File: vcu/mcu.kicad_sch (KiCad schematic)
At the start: 45 parts, among them J16 Spare pins, J7 Conn_ARM_JTAG_SWD_20, SW1 SW_Push, SW2 SW_SPDT, U7 STM32F746ZGT6, U8 LD1117S33TR_SOT223, Y1 8MHz

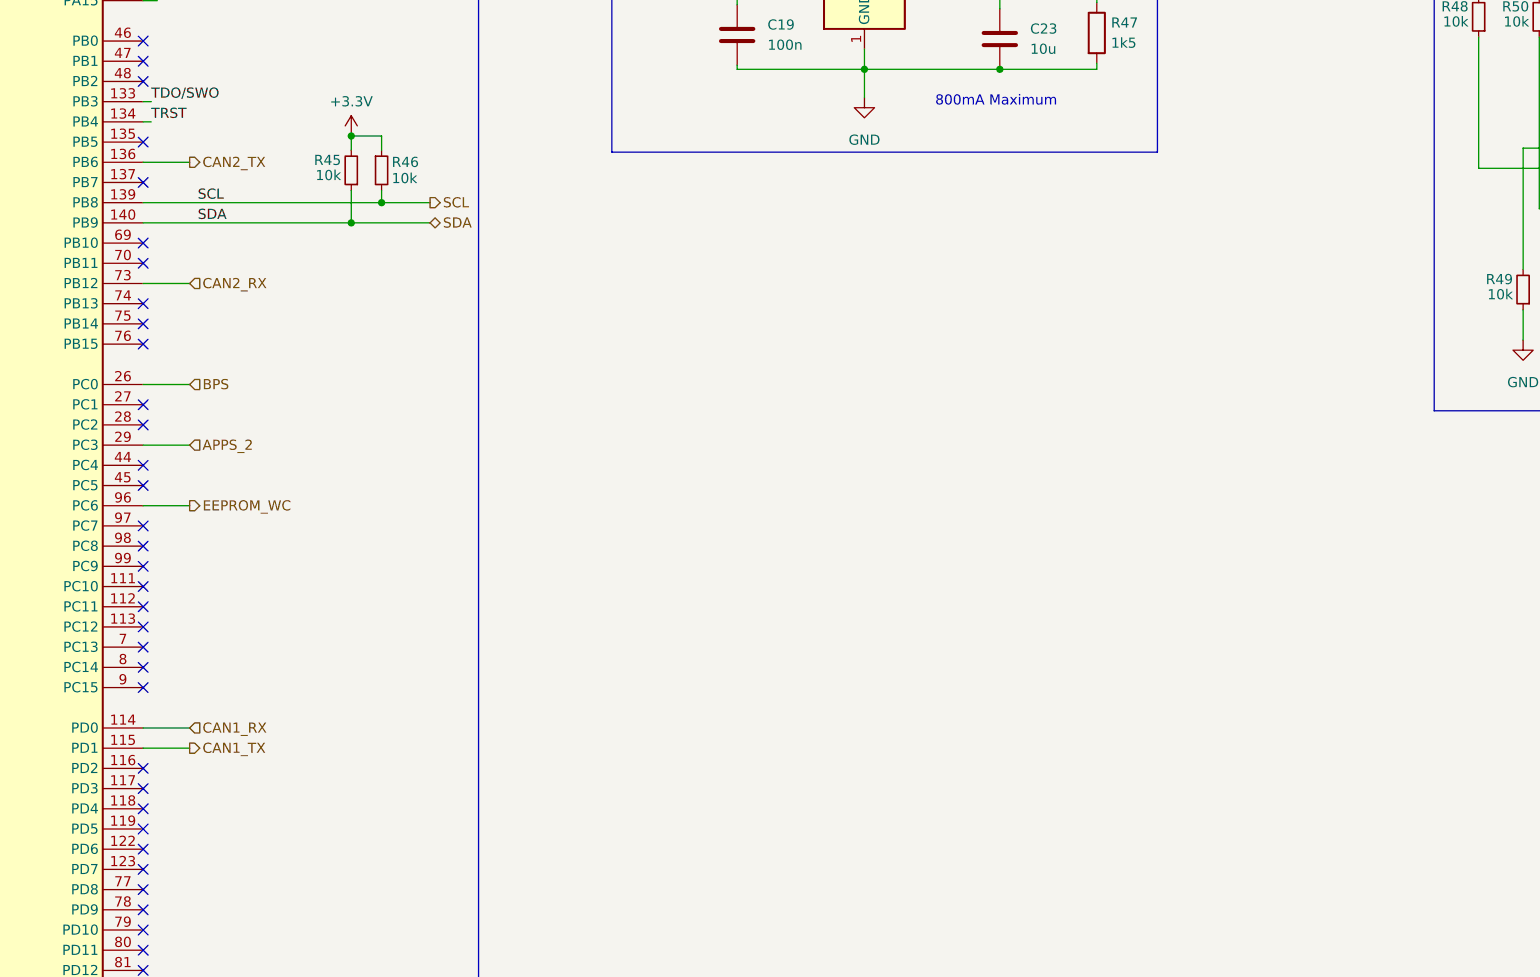
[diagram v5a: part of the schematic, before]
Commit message: Fixed CAN
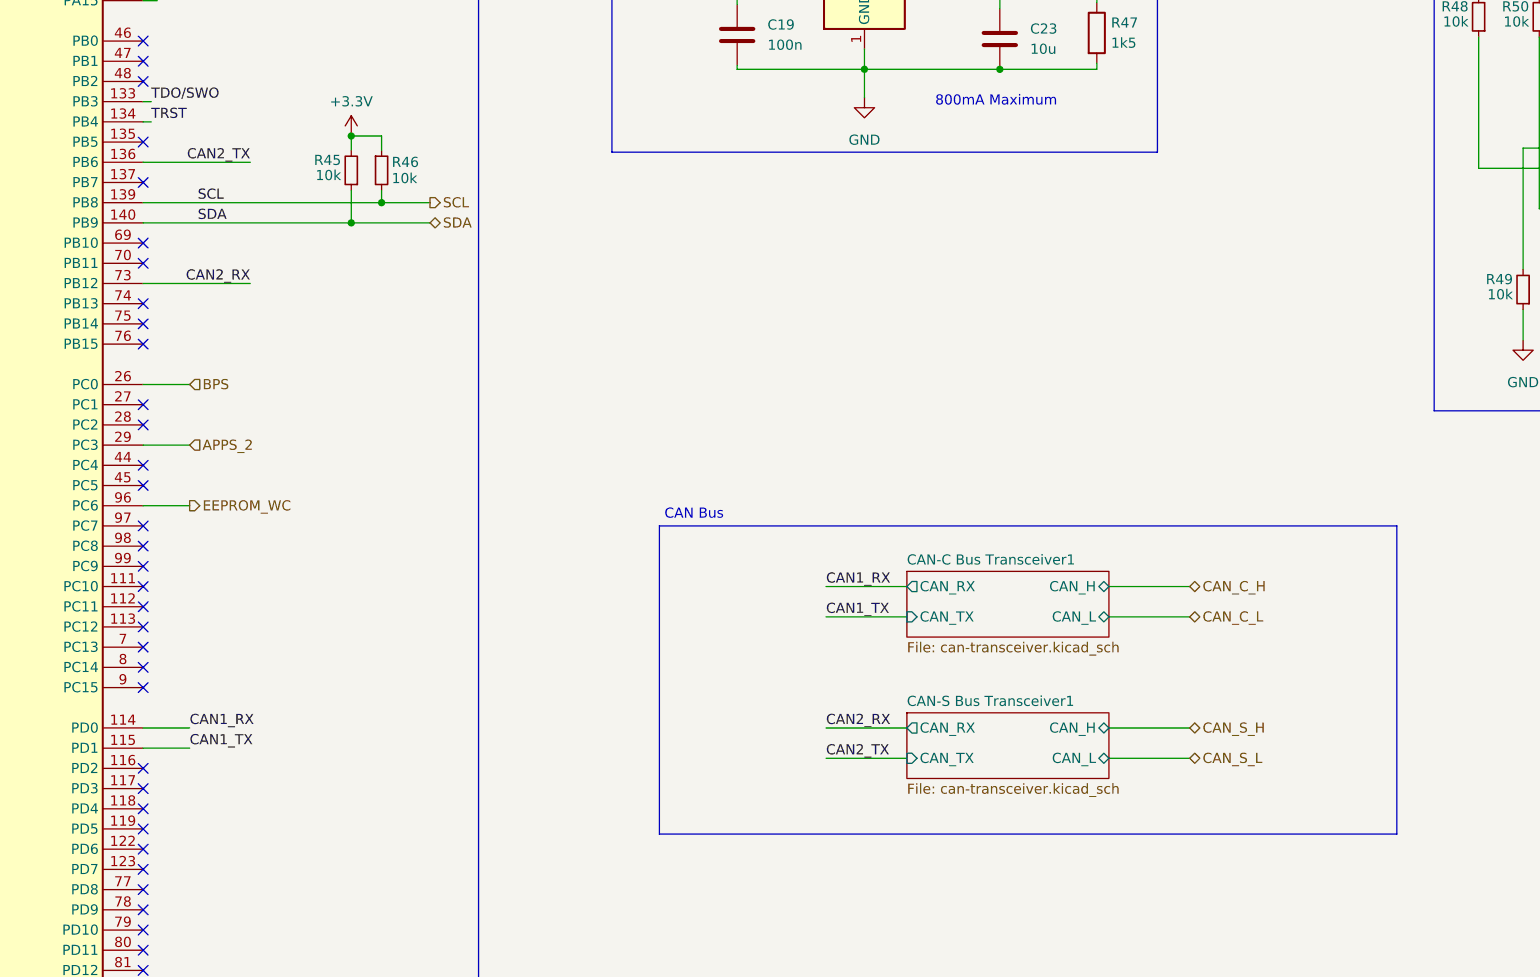
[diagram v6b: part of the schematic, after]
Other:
- added sheet CAN-C Bus Transceiver1 (can-transceiver.kicad_sch)
- added sheet CAN-S Bus Transceiver1 (can-transceiver.kicad_sch)
- note added: "CAN Bus"
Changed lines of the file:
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@@
     (stroke (width 0) (type default))
   )
-  (wire (pts (xy 138.938 102.87) (xy 144.78 102.87))
+  (wire (pts (xy 138.938 102.87) (xy 152.4 102.87))
     (stroke (width 0) (type default))
   )
@@
     (stroke (width 0) (type default))
   )
+  (wire (pts (xy 224.79 156.21) (xy 234.95 156.21))
+    (stroke (width 0) (type default))
+  )
   (wire (pts (xy 72.136 184.15) (xy 77.978 184.15))
     (stroke (width 0) (type default))
   )
+  (wire (pts (xy 260.35 173.99) (xy 270.51 173.99))
+    (stroke (width 0) (type default))
+  )
   (wire (pts (xy 95.758 34.036) (xy 95.758 36.83))
     (stroke (width 0) (type default))
   )
+  (wire (pts (xy 224.79 160.02) (xy 234.95 160.02))
+    (stroke (width 0) (type default))
+  )
   (wire (pts (xy 138.938 110.49) (xy 165.1 110.49))
     (stroke (width 0) (type default))
@@
     (stroke (width 0) (type default))
   )
+  (polyline (pts (xy 203.835 148.59) (xy 296.545 148.59))
+    (stroke (width 0) (type default))
+  )
   (wire (pts (xy 251.46 34.29) (xy 251.46 30.988))
     (stroke (width 0) (type default))
@@
     (stroke (width 0) (type default))
   )
+  (polyline (pts (xy 203.835 187.325) (xy 203.835 148.59))
+    (stroke (width 0) (type default))
+  )
   (wire (pts (xy 241.554 34.29) (xy 241.554 30.988))
     (stroke (width 0) (type default))
@@
     (stroke (width 0) (type default))
   )
-  (wire (pts (xy 138.938 118.11) (xy 144.78 118.11))
+  (wire (pts (xy 138.938 118.11) (xy 152.4 118.11))
     (stroke (width 0) (type default))
   )
@@
     (stroke (width 0) (type default))
   )
+  (polyline (pts (xy 296.545 148.59) (xy 296.545 187.325))
+    (stroke (width 0) (type default))
+  )
   (wire (pts (xy 205.486 41.91) (xy 205.486 44.958))
     (stroke (width 0) (type default))
@@
     (stroke (width 0) (type default))
   )
+  (wire (pts (xy 224.79 177.8) (xy 234.95 177.8))
+    (stroke (width 0) (type default))
+  )
   (wire (pts (xy 205.486 30.988) (xy 213.36 30.988))
     (stroke (width 0) (type default))
@@
     (stroke (width 0) (type default))
   )
+  (wire (pts (xy 260.35 177.8) (xy 270.51 177.8))
+    (stroke (width 0) (type default))
+  )
   (wire (pts (xy 280.67 44.958) (xy 270.764 44.958))
     (stroke (width 0) (type default))
@@
     (stroke (width 0) (type default))
   )
+  (polyline (pts (xy 296.545 187.325) (xy 203.835 187.325))
+    (stroke (width 0) (type default))
+  )
   (wire (pts (xy 348.996 81.026) (xy 348.996 81.788))
     (stroke (width 0) (type default))
@@
     (stroke (width 0) (type default))
   )
+  (wire (pts (xy 224.79 173.99) (xy 234.95 173.99))
+    (stroke (width 0) (type default))
+  )
   (wire (pts (xy 223.266 30.988) (xy 223.266 34.29))
     (stroke (width 0) (type default))
@@
   )
   (wire (pts (xy 321.056 82.042) (xy 321.056 80.518))
+    (stroke (width 0) (type default))
+  )
+  (wire (pts (xy 260.35 160.02) (xy 270.51 160.02))
+    (stroke (width 0) (type default))
+  )
+  (wire (pts (xy 260.35 156.21) (xy 270.51 156.21))
     (stroke (width 0) (type default))
   )
@@
     (effects (font (size 1.27 1.27)) (justify left bottom))
   )
+  (text "CAN Bus" (at 204.47 147.955 0)
+    (effects (font (size 1.27 1.27)) (justify left bottom))
+  )
   (text "ARM 20-Pin JTAG(5-bits)/Serial Wire Debugger" (at 301.244 69.342 0)
     (effects (font (size 1.27 1.27)) (justify left bottom))
@@
     (effects (font (size 1.27 1.27)) (justify left bottom))
   )
+  (label "CAN1_TX" (at 144.78 176.53 0) (fields_autoplaced)
+    (effects (font (size 1.27 1.27)) (justify left bottom))
+  )
   (label "NRST" (at 328.676 93.472 180) (fields_autoplaced)
     (effects (font (size 1.27 1.27)) (justify right bottom))
@@
     (effects (font (size 1.27 1.27)) (justify right bottom))
   )
+  (label "CAN2_TX" (at 224.79 177.8 0) (fields_autoplaced)
+    (effects (font (size 1.27 1.27)) (justify left bottom))
+  )
   (label "TDO{slash}SWO" (at 139.954 95.25 0) (fields_autoplaced)
     (effects (font (size 1.27 1.27)) (justify left bottom))
@@
     (effects (font (size 1.27 1.27)) (justify right bottom))
   )
+  (label "CAN2_TX" (at 152.4 102.87 180) (fields_autoplaced)
+    (effects (font (size 1.27 1.27)) (justify right bottom))
+  )
   (label "TCK{slash}SWDCLK" (at 328.676 101.092 180) (fields_autoplaced)
     (effects (font (size 1.27 1.27)) (justify right bottom))
   )
+  (label "CAN2_RX" (at 152.4 118.11 180) (fields_autoplaced)
+    (effects (font (size 1.27 1.27)) (justify right bottom))
+  )
+  (label "CAN1_RX" (at 144.78 173.99 0) (fields_autoplaced)
+    (effects (font (size 1.27 1.27)) (justify left bottom))
+  )
+  (label "CAN2_RX" (at 224.79 173.99 0) (fields_autoplaced)
+    (effects (font (size 1.27 1.27)) (justify left bottom))
+  )
   (label "TMS{slash}SWDIO" (at 140.716 77.47 0) (fields_autoplaced)
     (effects (font (size 1.27 1.27)) (justify left bottom))
   )
+  (label "CAN1_RX" (at 224.79 156.21 0) (fields_autoplaced)
+    (effects (font (size 1.27 1.27)) (justify left bottom))
+  )
   (label "TMS{slash}SWDIO" (at 328.676 103.632 180) (fields_autoplaced)
     (effects (font (size 1.27 1.27)) (justify right bottom))
@@
     (effects (font (size 1.27 1.27)) (justify left bottom))
   )
+  (label "CAN1_TX" (at 224.79 160.02 0) (fields_autoplaced)
+    (effects (font (size 1.27 1.27)) (justify left bottom))
+  )
   (hierarchical_label "SHDN" (shape input) (at 72.136 115.57 180) (fields_autoplaced)
     (effects (font (size 1.27 1.27)) (justify right))
@@
     (effects (font (size 1.27 1.27)) (justify right))
   )
-  (hierarchical_label "CAN2_RX" (shape input) (at 144.78 118.11 0) (fields_autoplaced)
-    (effects (font (size 1.27 1.27)) (justify left))
-  )
   (hierarchical_label "TS_ON" (shape output) (at 72.136 148.59 180) (fields_autoplaced)
     (effects (font (size 1.27 1.27)) (justify right))
@@
     (effects (font (size 1.27 1.27)) (justify right))
   )
+  (hierarchical_label "CAN_C_L" (shape tri_state) (at 270.51 160.02 0) (fields_autoplaced)
+    (effects (font (size 1.27 1.27)) (justify left))
+  )
   (hierarchical_label "STATUS" (shape output) (at 72.136 179.07 180) (fields_autoplaced)
     (effects (font (size 1.27 1.27)) (justify right))
   )
-  (hierarchical_label "CAN2_TX" (shape output) (at 144.78 102.87 0) (fields_autoplaced)
-    (effects (font (size 1.27 1.27)) (justify left))
-  )
   (hierarchical_label "TS_ON_BTN" (shape input) (at 72.136 125.73 180) (fields_autoplaced)
     (effects (font (size 1.27 1.27)) (justify right))
   )
-  (hierarchical_label "CAN1_TX" (shape output) (at 144.78 176.53 0) (fields_autoplaced)
-    (effects (font (size 1.27 1.27)) (justify left))
-  )
   (hierarchical_label "DRS" (shape output) (at 144.78 44.45 0) (fields_autoplaced)
     (effects (font (size 1.27 1.27)) (justify left))
   )
-  (hierarchical_label "CAN1_RX" (shape input) (at 144.78 173.99 0) (fields_autoplaced)
+  (hierarchical_label "CAN_S_L" (shape tri_state) (at 270.51 177.8 0) (fields_autoplaced)
+    (effects (font (size 1.27 1.27)) (justify left))
+  )
+  (hierarchical_label "CAN_S_H" (shape tri_state) (at 270.51 173.99 0) (fields_autoplaced)
     (effects (font (size 1.27 1.27)) (justify left))
   )
   (hierarchical_label "R2D_SIREN" (shape output) (at 72.136 151.13 180) (fields_autoplaced)
     (effects (font (size 1.27 1.27)) (justify right))
+  )
+  (hierarchical_label "CAN_C_H" (shape tri_state) (at 270.51 156.21 0) (fields_autoplaced)
+    (effects (font (size 1.27 1.27)) (justify left))
   )
   (hierarchical_label "APPS_1" (shape input) (at 144.78 52.07 0) (fields_autoplaced)
@@
       )
     )
+  )
+  (sheet (at 234.95 172.085) (size 25.4 8.255) (fields_autoplaced)
+    (stroke (width 0.1524) (type solid))
+    (fill (color 0 0 0 0.0000))
+    (property "Sheetname" "CAN-S Bus Transceiver1" (at 234.95 171.3734 0)
+      (effects (font (size 1.27 1.27)) (justify left bottom))
+    )
+    (property "Sheetfile" "can-transceiver.kicad_sch" (at 234.95 180.9246 0)
+      (effects (font (size 1.27 1.27)) (justify left top))
+    )
+    (pin "CAN_L" bidirectional (at 260.35 177.8 0)
+      (effects (font (size 1.27 1.27)) (justify right))
+    )
+    (pin "CAN_H" bidirectional (at 260.35 173.99 0)
+      (effects (font (size 1.27 1.27)) (justify right))
+    )
+    (pin "CAN_RX" output (at 234.95 173.99 180)
+      (effects (font (size 1.27 1.27)) (justify left))
+    )
+    (pin "CAN_TX" input (at 234.95 177.8 180)
+      (effects (font (size 1.27 1.27)) (justify left))
+    )
+    (instances
+      (project "vcu"
+        (path "/d2151cc9-0acc-4d18-a050-63c63ade8261" (page "3"))
+        (path "/d2151cc9-0acc-4d18-a050-63c63ade8261/b7d12d3a-f9ac-4555-ba71-8dba49820627" (page "4"))
+      )
+    )
+  )
+  (sheet (at 234.95 154.305) (size 25.4 8.255) (fields_autoplaced)
+    (stroke (width 0.1524) (type solid))
+    (fill (color 0 0 0 0.0000))
+    (property "Sheetname" "CAN-C Bus Transceiver1" (at 234.95 153.5934 0)
+      (effects (font (size 1.27 1.27)) (justify left bottom))
+    )
+    (property "Sheetfile" "can-transceiver.kicad_sch" (at 234.95 163.1446 0)
+      (effects (font (size 1.27 1.27)) (justify left top))
+    )
+    (pin "CAN_L" bidirectional (at 260.35 160.02 0)
+      (effects (font (size 1.27 1.27)) (justify right))
+    )
+    (pin "CAN_H" bidirectional (at 260.35 156.21 0)
+      (effects (font (size 1.27 1.27)) (justify right))
+    )
+    (pin "CAN_RX" output (at 234.95 156.21 180)
+      (effects (font (size 1.27 1.27)) (justify left))
+    )
+    (pin "CAN_TX" input (at 234.95 160.02 180)
+      (effects (font (size 1.27 1.27)) (justify left))
+    )
+    (instances
+      (project "vcu"
+        (path "/d2151cc9-0acc-4d18-a050-63c63ade8261" (page "2"))
+        (path "/d2151cc9-0acc-4d18-a050-63c63ade8261/b7d12d3a-f9ac-4555-ba71-8dba49820627" (page "9"))
+      )
+    )

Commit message: Tweaks, fixing CAN
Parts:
- removed Y1: 8MHz, Crystal:Crystal_HC49-U_Vertical, symbol Device:Crystal
- added Y4: 8MHz, Crystal:Crystal_SMD_3225-4Pin_3.2x2.5mm_HandSoldering, symbol Device:Crystal_GND24
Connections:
- net GND: now also Y4.2, Y4.4
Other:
- sheet CAN-C Bus Transceiver1 ports: added CAN_3V3; removed none
- sheet CAN-S Bus Transceiver1 ports: added CAN_3V3; removed none

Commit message: Added Order Codes
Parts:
- J7: Order Code (none) -> 649-75869-104LF
- U7: Order Code (none) -> 511-STM32F746ZGT6
- U8: Order Code (none) -> 511-LD1117S33
- Y4: Order Code (none) -> 815-FC3BAEBDI8.0-T1
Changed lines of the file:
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@@
       (effects (font (size 1.27 1.27)))
+    )
+    (property "Order Code" "511-LD1117S33" (at 229.616 81.026 0)
+      (effects (font (size 1.27 1.27)) hide)
     )
     (pin "1")
@@
     )
     (property "Datasheet" "~" (at 60.96 71.755 0)
+      (effects (font (size 1.27 1.27)) hide)
+    )
+    (property "Order Code" "815-FC3BAEBDI8.0-T1" (at 60.96 71.755 0)
       (effects (font (size 1.27 1.27)) hide)
     )
@@
     )
     (property "Datasheet" "http://infocenter.arm.com/help/topic/com.arm.doc.dui0499b/DUI0499B_system_design_reference.pdf" (at 355.346 135.382 90)
+      (effects (font (size 1.27 1.27)) hide)
+    )
+    (property "Order Code" "649-75869-104LF" (at 346.456 103.632 0)
       (effects (font (size 1.27 1.27)) hide)
     )
@@
       (effects (font (size 1.27 1.27)) hide)
     )
+    (property "Order Code" "511-STM32F746ZGT6" (at 108.458 130.81 0)
+      (effects (font (size 1.27 1.27)) hide)
+    )
